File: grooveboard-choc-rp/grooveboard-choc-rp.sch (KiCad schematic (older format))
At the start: 41 parts, among them J1 USB_C_Receptacle_USB2.0, K1 MX-NoLED, K2 MX-NoLED, K3 MX-NoLED, K4 MX-NoLED, SW1 BOOT, SW2 RESET, U1 RP2040, U2 W25Q128JV, U3 AP2112K-3.3, Y1 12MHz

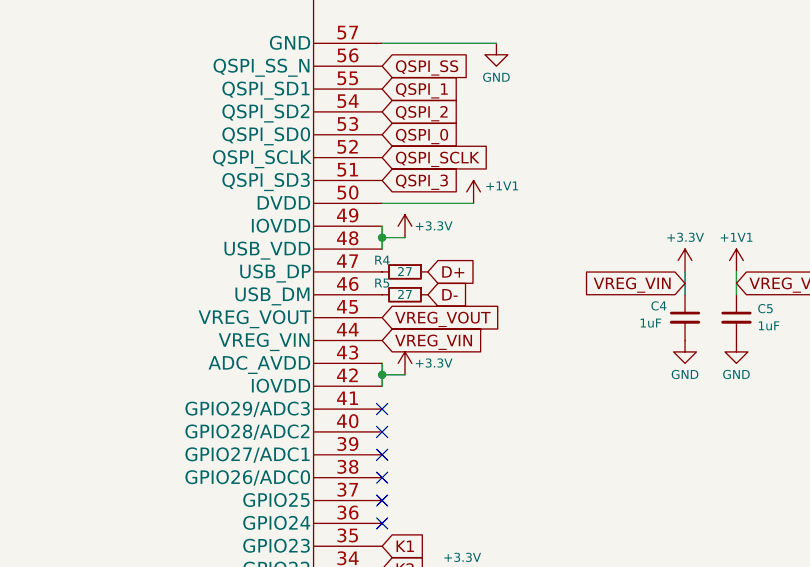
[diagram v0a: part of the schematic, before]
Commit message: update usb resistors
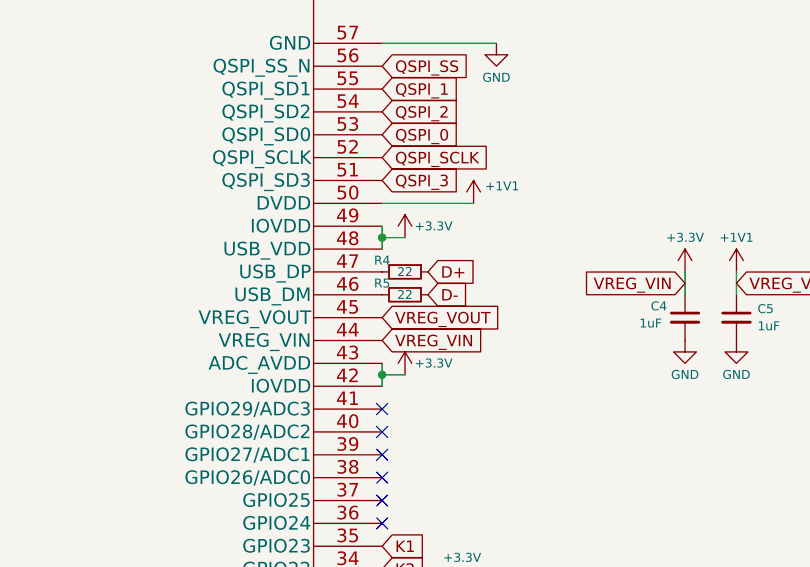
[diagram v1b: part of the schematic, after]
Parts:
- R4, R5: value 27 -> 22
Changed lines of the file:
@@
 P 7800 2200
 F 0 "R4" V 7750 2100 39  0000 C CNN
-F 1 "27" V 7800 2200 39  0000 C CNN
+F 1 "22" V 7800 2200 39  0000 C CNN
 F 2 "Keebio-Parts:R_0402" H 7800 2200 50  0001 C CNN
 F 3 "~" H 7800 2200 50  0001 C CNN
@@
 P 7800 2300
 F 0 "R5" V 7750 2200 39  0000 C CNN
-F 1 "27" V 7800 2300 39  0000 C CNN
+F 1 "22" V 7800 2300 39  0000 C CNN
 F 2 "Keebio-Parts:R_0402" H 7800 2300 50  0001 C CNN
 F 3 "~" H 7800 2300 50  0001 C CNN
